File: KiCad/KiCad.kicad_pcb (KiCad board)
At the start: 2 copper layers, 39.4 x 34.8 mm, 32 parts, among them J1 Conn_01x04_Male, J2 Conn_01x04_Male, J3 Conn_01x04_Male, J4 USB_B_Micro, SW1 SW_SPDT, U1 AMS1117-3.3, U2 STM32F103C8T6, Y1 Crystal_GND24

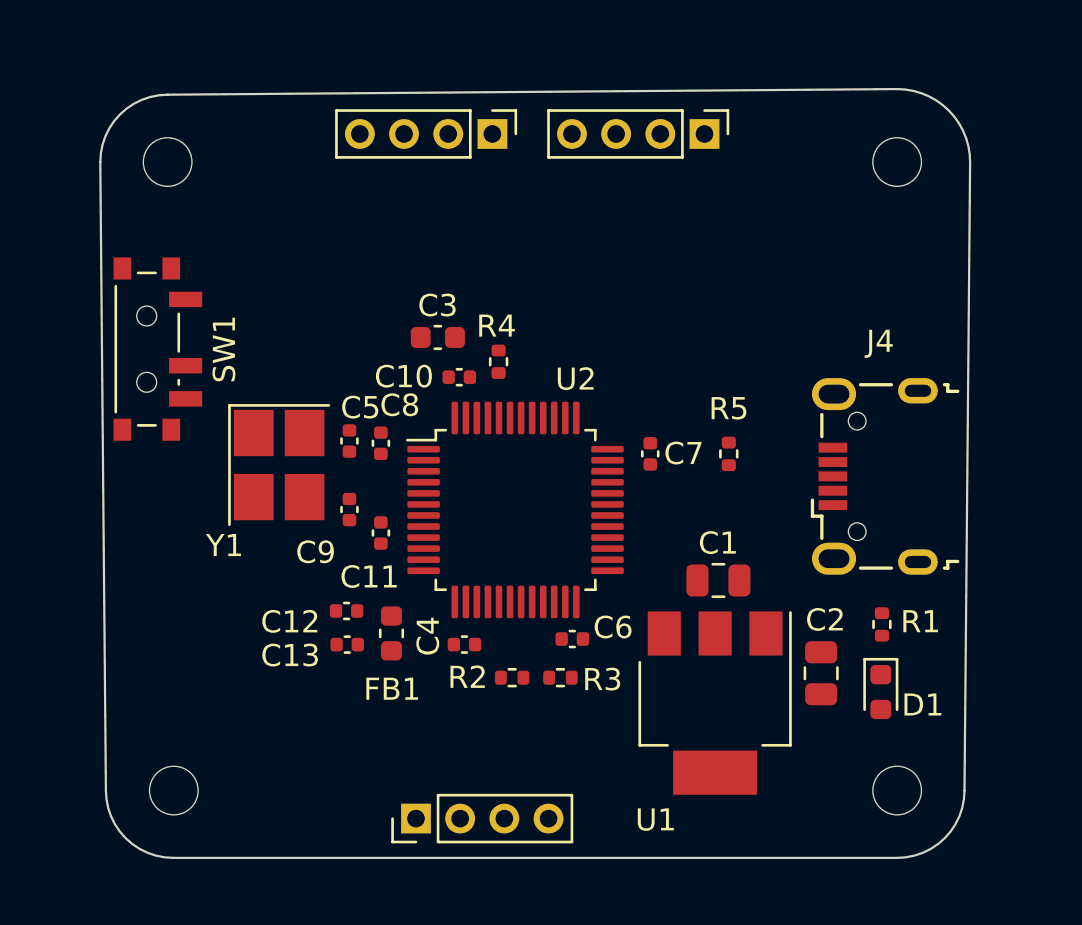
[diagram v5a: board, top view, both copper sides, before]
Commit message: Routed the sensitive components
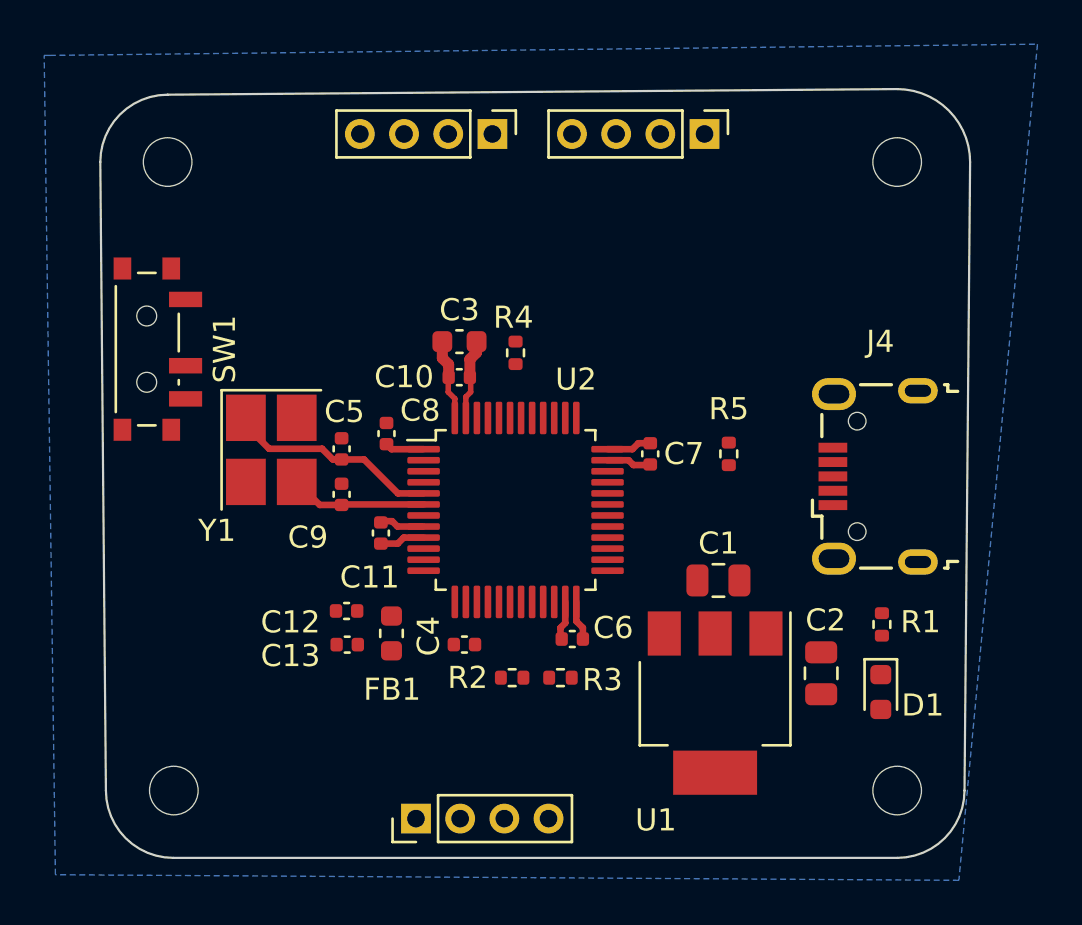
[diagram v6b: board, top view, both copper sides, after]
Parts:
- moved C3 1.00 mm to (122.4, 81.8)
- moved R4 0.87 mm to (125.0, 82.3)
- moved C9 0.77 mm to (117.1, 88.7)
- moved Y1 0.77 mm to (113.9, 86.7)
- moved C8 0.51 mm to (119.1, 86.0)
- moved C5 0.50 mm to (117.1, 86.6)
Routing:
- net /HSE_IN: track 0.00 -> 9.67 mm
- net GND: track 0.00 -> 9.57 mm
- net +3.3V: track 0.00 -> 9.33 mm
- net /HSE_OUT: track 0.00 -> 6.19 mm
- net +3.3VA: track 0.00 -> 2.05 mm
- added copper zone on B.Cu, net GND
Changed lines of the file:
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@@
   )
   (footprint "Capacitor_SMD:C_0603_1608Metric" (layer "F.Cu")
-    (at 121.45 81.6)
+    (at 122.428 81.788)
     (descr "Capacitor SMD 0603 (1608 Metric), square (rectangular) end terminal, IPC_7351 nominal, (Body size source: IPC-SM-782 page 76, https://www.pcb-3d.com/wordpress/wp-content/uploads/ipc-sm-782a_amendment_1_and_2.pdf), generated with kicad-footprint-generator")
     (tags "capacitor")
@@
   )
   (footprint "Resistor_SMD:R_0402_1005Metric" (layer "F.Cu")
-    (at 124.2 82.7 -90)
+    (at 124.968 82.296 -90)
     (descr "Resistor SMD 0402 (1005 Metric), square (rectangular) end terminal, IPC_7351 nominal, (Body size source: IPC-SM-782 page 72, https://www.pcb-3d.com/wordpress/wp-content/uploads/ipc-sm-782a_amendment_1_and_2.pdf), generated with kicad-footprint-generator")
     (tags "resistor")
@@
   )
   (footprint "Capacitor_SMD:C_0402_1005Metric" (layer "F.Cu")
-    (at 117.4496 89.3904 90)
+    (at 117.094 88.702 90)
     (descr "Capacitor SMD 0402 (1005 Metric), square (rectangular) end terminal, IPC_7351 nominal, (Body size source: IPC-SM-782 page 76, https://www.pcb-3d.com/wordpress/wp-content/uploads/ipc-sm-782a_amendment_1_and_2.pdf), generated with kicad-footprint-generator")
     (tags "capacitor")
@@
   )
   (footprint "Capacitor_SMD:C_0402_1005Metric" (layer "F.Cu")
-    (at 117.4496 86.2864 90)
+    (at 117.094 86.642 90)
     (descr "Capacitor SMD 0402 (1005 Metric), square (rectangular) end terminal, IPC_7351 nominal, (Body size source: IPC-SM-782 page 76, https://www.pcb-3d.com/wordpress/wp-content/uploads/ipc-sm-782a_amendment_1_and_2.pdf), generated with kicad-footprint-generator")
     (tags "capacitor")
@@
     (property "Sheetname" "")
     (attr smd)
-    (fp_text reference "C5" (at 1.496 0.508) (layer "F.SilkS")
+    (fp_text reference "C5" (at 1.679 0.127) (layer "F.SilkS")
       (effects (font (size 1 1) (thickness 0.15)))
     )
@@
   )
   (footprint "Crystal:Crystal_SMD_3225-4Pin_3.2x2.5mm_HandSoldering" (layer "F.Cu")
-    (at 114.2676 87.3764 -90)
+    (at 113.912 86.688 -90)
     (descr "SMD Crystal SERIES SMD3225/4 http://www.txccrystal.com/images/pdf/7m-accuracy.pdf, hand-soldering, 3.2x2.5mm^2 package")
     (tags "SMD SMT crystal hand-soldering")
@@
   )
   (footprint "Capacitor_SMD:C_0402_1005Metric" (layer "F.Cu")
-    (at 118.872 86.388 90)
+    (at 119.126 85.951 90)
     (descr "Capacitor SMD 0402 (1005 Metric), square (rectangular) end terminal, IPC_7351 nominal, (Body size source: IPC-SM-782 page 76, https://www.pcb-3d.com/wordpress/wp-content/uploads/ipc-sm-782a_amendment_1_and_2.pdf), generated with kicad-footprint-generator")
     (tags "capacitor")
@@
     (property "Sheetname" "")
     (attr smd)
-    (fp_text reference "C8" (at 1.7044 0.8636) (layer "F.SilkS")
+    (fp_text reference "C8" (at 1.044 1.524) (layer "F.SilkS")
       (effects (font (size 1 1) (thickness 0.15)))
     )
@@
   (gr_arc (start 142.24 70.358) (mid 144.574867 71.325133) (end 145.542 73.66) (layer "Edge.Cuts") (width 0.1))
   (gr_line (start 145.288 102.108) (end 145.542 73.66) (layer "Edge.Cuts") (width 0.1))
+  (segment (start 127.218 93.5705) (end 127.218 94.524) (width 0.3) (layer "F.Cu") (net 2))
+  (segment (start 123.203 81.788) (end 123.203 82.283) (width 0.5) (layer "F.Cu") (net 2))
+  (segment (start 127 95.194) (end 127.056 95.25) (width 0.3) (layer "F.Cu") (net 2))
+  (segment (start 122.936 83.436) (end 122.9 83.4) (width 0.25) (layer "F.Cu") (net 2))
+  (segment (start 130.084 87.158) (end 130.302 87.376) (width 0.3) (layer "F.Cu") (net 2))
+  (segment (start 130.302 87.376) (end 131.036 87.376) (width 0.3) (layer "F.Cu") (net 2))
+  (segment (start 119.622 90.158) (end 119.38 89.916) (width 0.3) (layer "F.Cu") (net 2))
+  (segment (start 118.928 89.916) (end 118.872 89.972) (width 0.3) (layer "F.Cu") (net 2))
+  (segment (start 129.1305 87.158) (end 130.084 87.158) (width 0.3) (layer "F.Cu") (net 2))
+  (segment (start 127 94.742) (end 127 95.194) (width 0.3) (layer "F.Cu") (net 2))
+  (segment (start 120.8055 90.158) (end 119.622 90.158) (width 0.3) (layer "F.Cu") (net 2))
+  (segment (start 122.9 82.586) (end 122.9 83.4) (width 0.5) (layer "F.Cu") (net 2))
+  (segment (start 122.718 84.292) (end 122.936 84.074) (width 0.25) (layer "F.Cu") (net 2))
+  (segment (start 123.203 82.283) (end 122.9 82.586) (width 0.5) (layer "F.Cu") (net 2))
+  (segment (start 127.218 94.524) (end 127 94.742) (width 0.3) (layer "F.Cu") (net 2))
+  (segment (start 122.936 84.074) (end 122.936 83.436) (width 0.25) (layer "F.Cu") (net 2))
+  (segment (start 119.38 89.916) (end 118.928 89.916) (width 0.3) (layer "F.Cu") (net 2))
+  (segment (start 131.036 87.376) (end 131.064 87.348) (width 0.3) (layer "F.Cu") (net 2))
+  (segment (start 122.718 85.2455) (end 122.718 84.292) (width 0.25) (layer "F.Cu") (net 2))
+  (segment (start 122.218 84.372) (end 121.92 84.074) (width 0.25) (layer "F.Cu") (net 3))
+  (segment (start 130.528 86.388) (end 131.064 86.388) (width 0.3) (layer "F.Cu") (net 3))
+  (segment (start 122.218 85.2455) (end 122.218 84.372) (width 0.25) (layer "F.Cu") (net 3))
+  (segment (start 127.718 93.5705) (end 127.718 94.444) (width 0.3) (layer "F.Cu") (net 3))
+  (segment (start 130.258 86.658) (end 130.528 86.388) (width 0.3) (layer "F.Cu") (net 3))
+  (segment (start 119.353 86.658) (end 119.126 86.431) (width 0.3) (layer "F.Cu") (net 3))
+  (segment (start 121.653 82.537) (end 121.94 82.824) (width 0.5) (layer "F.Cu") (net 3))
+  (segment (start 128.016 94.742) (end 128.016 95.25) (width 0.3) (layer "F.Cu") (net 3))
+  (segment (start 121.92 83.42) (end 121.94 83.4) (width 0.25) (layer "F.Cu") (net 3))
+  (segment (start 121.92 84.074) (end 121.92 83.42) (width 0.25) (layer "F.Cu") (net 3))
+  (segment (start 121.94 82.824) (end 121.94 83.4) (width 0.5) (layer "F.Cu") (net 3))
+  (segment (start 129.1305 86.658) (end 130.258 86.658) (width 0.3) (layer "F.Cu") (net 3))
+  (segment (start 120.8055 86.658) (end 119.353 86.658) (width 0.3) (layer "F.Cu") (net 3))
+  (segment (start 121.653 81.788) (end 121.653 82.537) (width 0.5) (layer "F.Cu") (net 3))
+  (segment (start 127.718 94.444) (end 128.016 94.742) (width 0.3) (layer "F.Cu") (net 3))
+  (segment (start 117.094 87.122) (end 116.696 87.122) (width 0.3) (layer "F.Cu") (net 5))
+  (segment (start 116.696 87.122) (end 116.212 86.638) (width 0.3) (layer "F.Cu") (net 5))
+  (segment (start 113.812 86.638) (end 112.762 85.588) (width 0.3) (layer "F.Cu") (net 5))
+  (segment (start 119.646 88.658) (end 118.11 87.122) (width 0.3) (layer "F.Cu") (net 5))
+  (segment (start 118.11 87.122) (end 117.094 87.122) (width 0.3) (layer "F.Cu") (net 5))
+  (segment (start 120.8055 88.658) (end 119.646 88.658) (width 0.3) (layer "F.Cu") (net 5))
+  (segment (start 116.212 86.638) (end 113.812 86.638) (width 0.3) (layer "F.Cu") (net 5))
+  (segment (start 112.762 85.588) (end 112.762 85.238) (width 0.3) (layer "F.Cu") (net 5))
+  (segment (start 117.094 89.182) (end 116.106 89.182) (width 0.3) (layer "F.Cu") (net 6))
+  (segment (start 120.8055 89.158) (end 117.118 89.158) (width 0.3) (layer "F.Cu") (net 6))
+  (segment (start 116.106 89.182) (end 115.062 88.138) (width 0.3) (layer "F.Cu") (net 6))
+  (segment (start 117.118 89.158) (end 117.094 89.182) (width 0.3) (layer "F.Cu") (net 6))
+  (segment (start 120.8055 90.658) (end 119.908 90.658) (width 0.3) (layer "F.Cu") (net 7))
+  (segment (start 119.908 90.658) (end 119.634 90.932) (width 0.3) (layer "F.Cu") (net 7))
+  (segment (start 119.634 90.932) (end 118.872 90.932) (width 0.3) (layer "F.Cu") (net 7))
+  (zone (net 2) (net_name "GND") (layer "B.Cu") (hatch edge 0.508)
+    (connect_pads (clearance 0.3))
+    (min_thickness 0.25) (filled_areas_thickness no)
+    (fill yes (thermal_gap 0.5) (thermal_bridge_width 0.5))
+    (polygon
+      (pts
+        (xy 145.034 106.172)
+        (xy 104.14 105.918)
+        (xy 103.632 68.834)
+        (xy 103.886 68.834)
+        (xy 148.59 68.326)
+      )
+    )
+  )
 )

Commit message: Routed Pinout Connectors & other signal pins
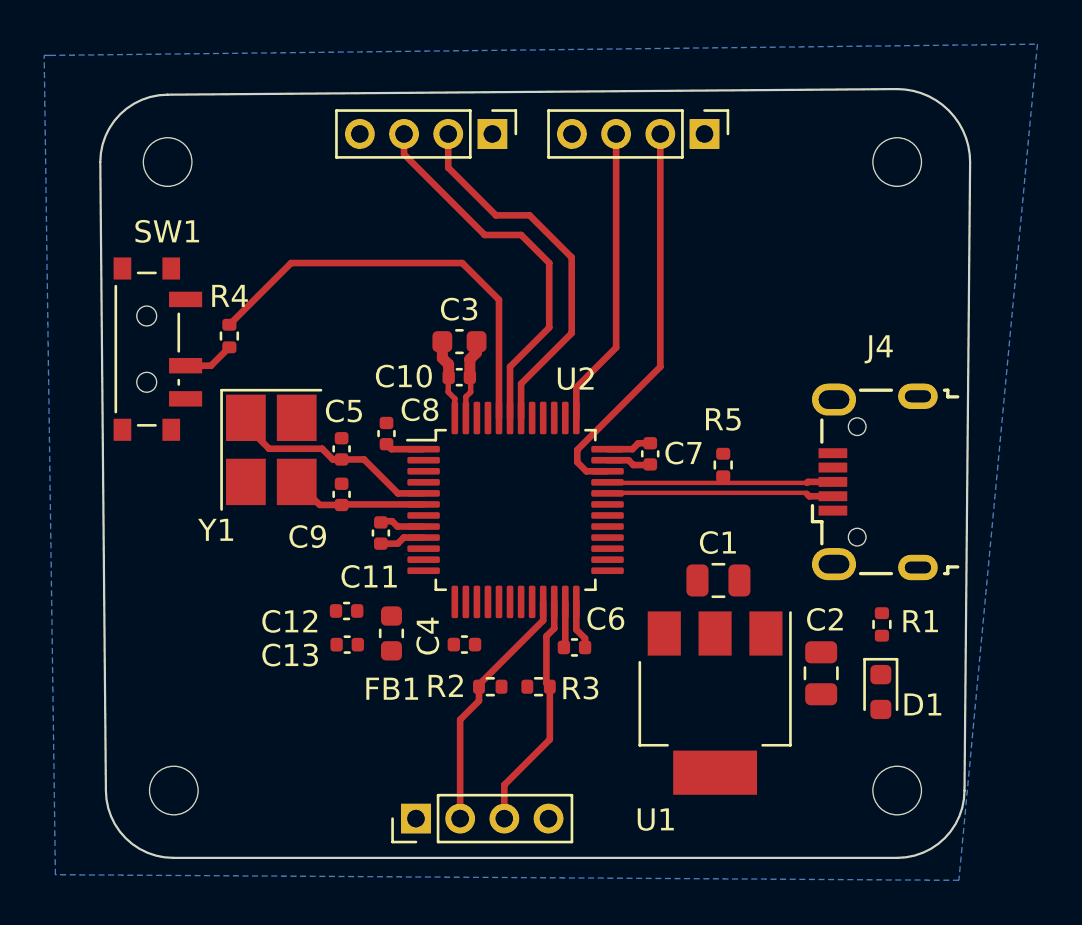
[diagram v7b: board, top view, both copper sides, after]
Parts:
- moved R4 13.0 mm to (112.0, 81.5), turned to 90 degrees
- moved R2 1.07 mm to (123.8, 97.4)
- moved R3 1.07 mm to (126.0, 97.4)
- moved R5 0.56 mm to (134.4, 87.4)
- moved C6 0.39 mm to (127.6, 95.6)
- moved J4 0.25 mm to (141.2, 88.1)
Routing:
- net /BOOT0: track 0.00 -> 19.4 mm
- net /SWDIO: track 0.00 -> 18.0 mm
- net /USART1_RX: track 0.00 -> 17.3 mm
- net /USART1_TX: track 0.00 -> 17.0 mm
- net /SWDCLK: track 0.00 -> 13.6 mm
- net /I2C2_SCL: track 0.00 -> 11.4 mm
- net /I2C2_SDA: track 0.00 -> 10.9 mm
- net /USB_D-: track 0.00 -> 10.3 mm
- net /USB_D+: track 0.00 -> 10.2 mm
- net /FW_BOOT0: track 0.00 -> 2.33 mm

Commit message: Finished Power Routing
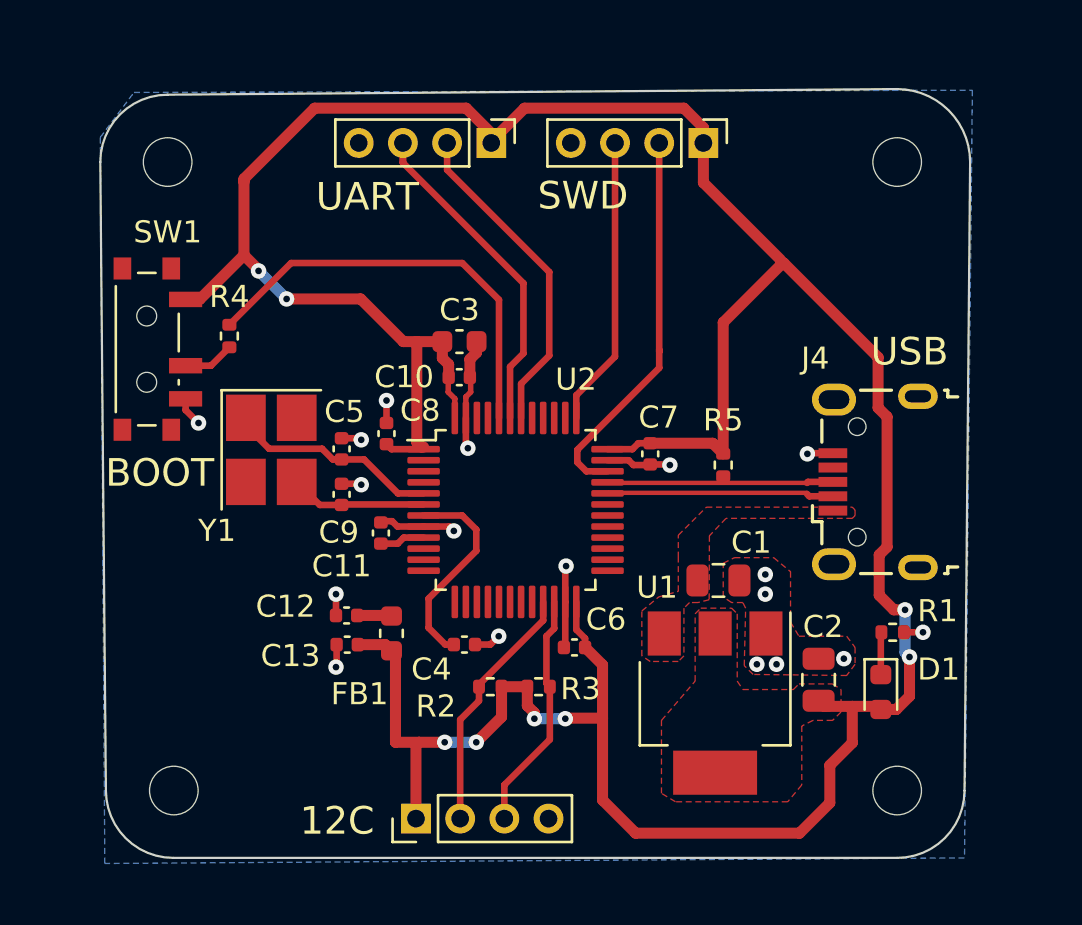
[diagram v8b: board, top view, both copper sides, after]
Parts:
- moved R1 0.60 mm to (142.0, 94.9), turned to 0 degrees
- moved J3 0.41 mm to (133.5, 72.8)
- moved J1 0.41 mm to (123.9, 72.8)
- moved C2 0.32 mm to (138.7, 97.1)
- moved C12 0.20 mm to (117.3, 94.2), turned to 180 degrees
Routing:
- net +3.3V: track 9.75 -> 149.6 mm, vias 0 -> 8
- net GND: track 9.87 -> 24.7 mm, vias 0 -> 18
- net /NRST: track 0.00 -> 9.45 mm
- net /USART1_TX: track 17.0 -> 14.9 mm
- net /Power_LED: track 0.00 -> 1.78 mm
- net +3.3VA: track 2.05 -> 3.61 mm
- net /USART1_RX: track 17.3 -> 15.9 mm
- added copper zone on F.Cu, net +3.3V
- added copper zone on F.Cu, net GND
- added copper zone on F.Cu, net VBUS
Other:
- board text added: "12C"
- board text added: "BOOT"
- board text added: "SWD"
- board text added: "UART"
- board text added: "USB"
- board text added: "V1.1 10/22"
